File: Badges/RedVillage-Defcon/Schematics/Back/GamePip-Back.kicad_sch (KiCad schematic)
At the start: 21 parts

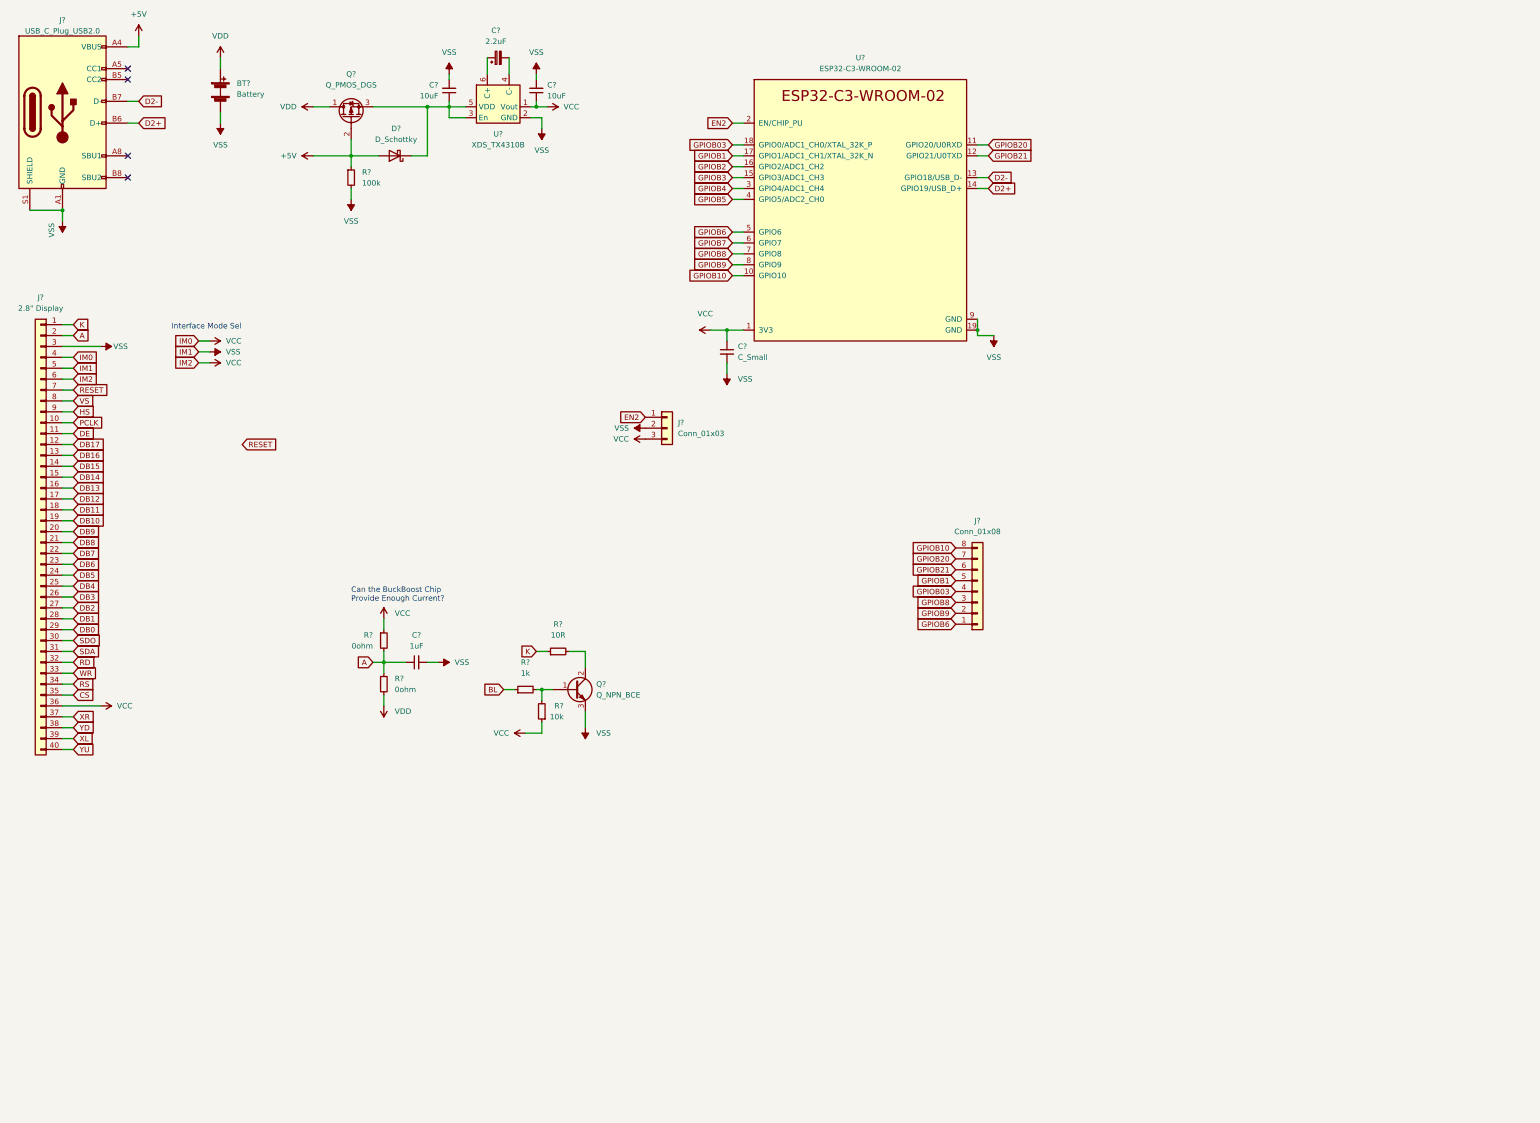
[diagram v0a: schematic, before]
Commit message: Changed RedVillage to ESP32-S2
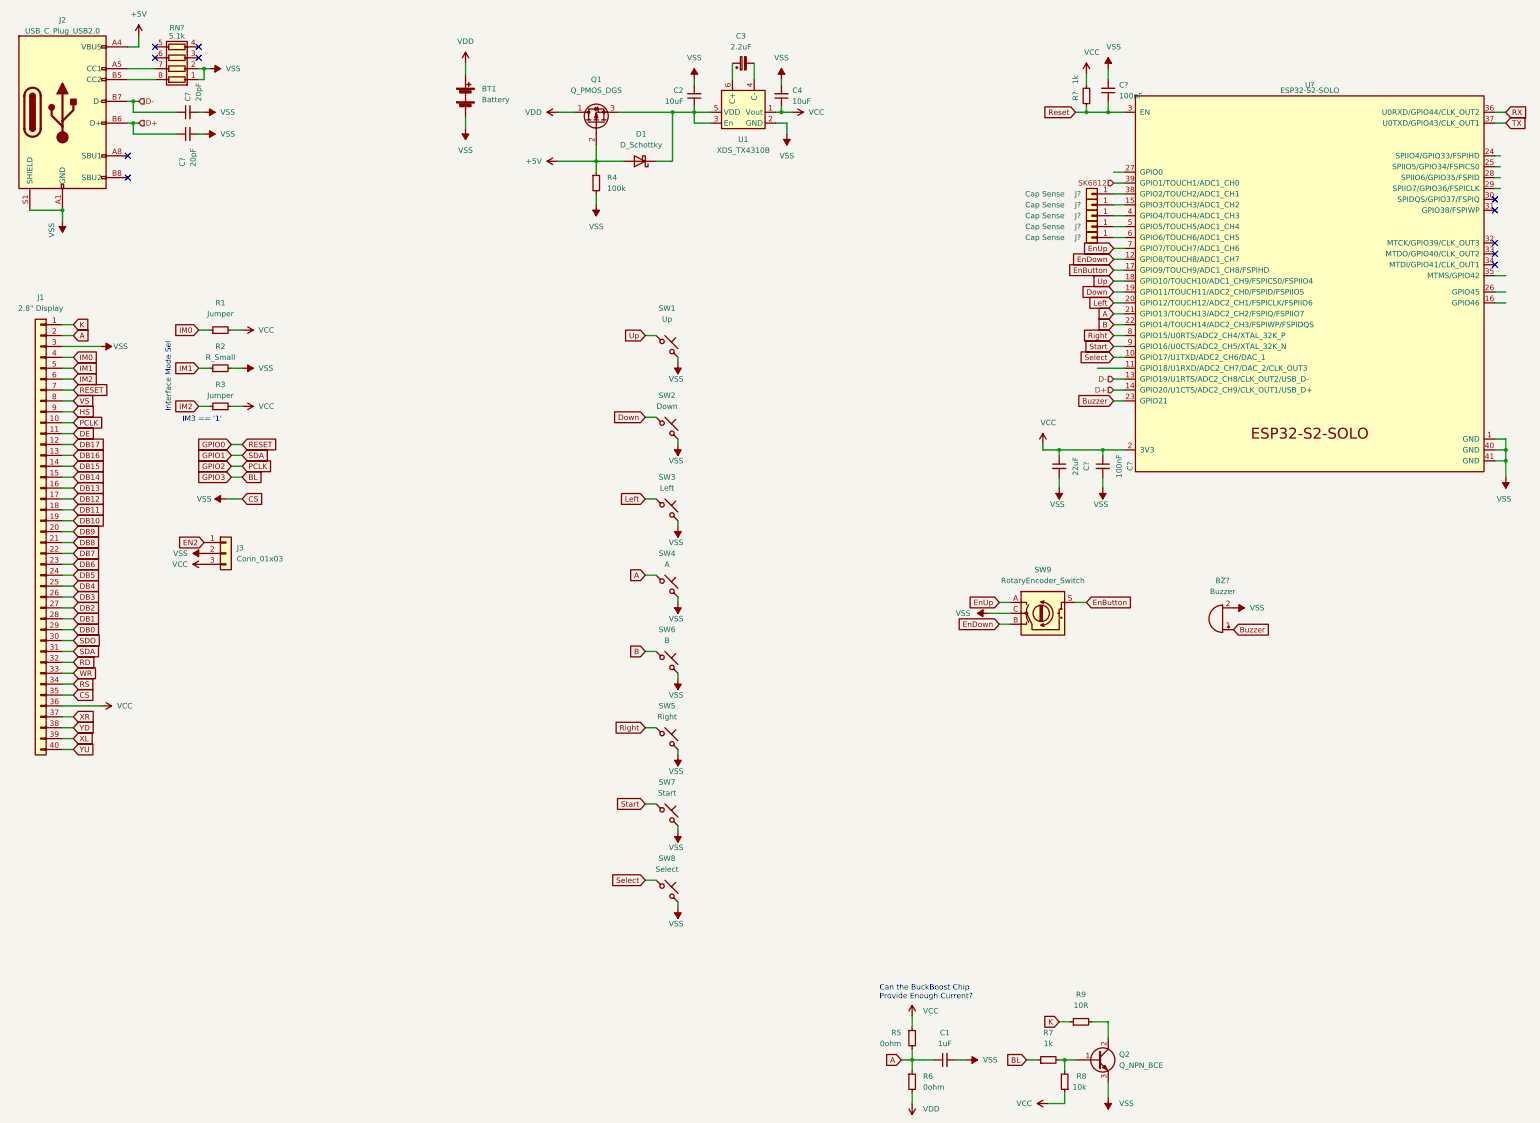
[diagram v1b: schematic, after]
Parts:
- removed C?: C_Small, Capacitor_SMD:C_0805_2012Metric, symbol Device:C_Small
- removed J?: Conn_01x08, Connector_PinHeader_2.54mm:PinHeader_1x08_P2.54mm_Vertical, symbol Connector_Generic:Conn_01x08
- removed U?: ESP32-C3-WROOM-02, Espressif:ESP32-C3-WROOM-02, symbol Espressif:ESP32-C3-WROOM-02
- added BZ?: Buzzer, Bsides22:FUET-9032-Buzzer, symbol Device:Buzzer
- added C? (x2): 100nF, Capacitor_SMD:C_0805_2012Metric, symbol Device:C_Small
- added C?: 22uF, Capacitor_SMD:C_0805_2012Metric, symbol Device:C_Small
- added C? (x2): 20pF, Capacitor_SMD:C_0805_2012Metric, symbol Device:C_Small
- added J? (x4): Cap Sense, Bsides22:CapSense, symbol Connector_Generic:Conn_01x01
- added J?: Cap Sense, CornConStranger:CapSence, symbol Connector_Generic:Conn_01x01
- added R1, R3: Jumper, symbol Device:R_Small
- added R2: R_Small, symbol Device:R_Small
- added R?: 1k, Resistor_SMD:R_0805_2012Metric, symbol Device:R_Small
- added RN?: 5.1k, Resistor_SMD:R_Array_Convex_4x0603, symbol Device:R_Pack04
- added SW1: Up, symbol Switch:SW_Push_45deg
- added SW2: Down, symbol Switch:SW_Push_45deg
- added SW3: Left, symbol Switch:SW_Push_45deg
- added SW4: A, symbol Switch:SW_Push_45deg
- added SW5: Right, symbol Switch:SW_Push_45deg
- added SW6: B, symbol Switch:SW_Push_45deg
- added SW7: Start, symbol Switch:SW_Push_45deg
- added SW8: Select, symbol Switch:SW_Push_45deg
- added SW9: RotaryEncoder_Switch, symbol RedVillage:RotaryEncoder_Switch
- added U?: ESP32-S2-SOLO, Espressif:ESP32-S2-SOLO, symbol Espressif:ESP32-S2-SOLO
- gave numbers to parts that had none: 18
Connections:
- net CS is gone; now on net VSS: J1.35 (Pin_35)
- net A: now also SW4.1, U?.21 (GPIO13/TOUCH13/ADC2_CH2/FSPIQ/FSPIIO7)
- net VCC: now also C?.1, C?.1, R1.2, R3.2, R?.2, U?.2 (3V3); no longer J1.4 (Pin_4), J1.6 (Pin_6)
- net VSS: now also BZ?.2 (+), C?.2, C?.2, C?.2, C?.2, C?.2, R2.2, RN?.1 (R1.1), RN?.2 (R2.1), SW1.2, SW2.2, SW3.2, SW4.2, SW5.2, SW6.2, SW7.2, SW8.2, SW9.C, U?.1 (GND), U?.40 (GND), U?.41 (GND); no longer J1.5 (Pin_5)
- net at J2.A5 (CC1): now also RN?.7 (R2.2)
- net at J2.B5 (CC2): now also RN?.8 (R1.2)
- net D2+ renamed D+
- net D+: now also C?.1, U?.14 (GPIO20/U1CTS/ADC2_CH9/CLK_OUT1/USB_D+)
- net D2- renamed D-
- net D-: now also C?.1, U?.13 (GPIO19/U1RTS/ADC2_CH8/CLK_OUT2/USB_D-)
- net PCLK renamed GPIO2
- net RESET renamed GPIO0
- net SDA renamed GPIO1
- new net: J?.1 (Pin_1), U?.6 (GPIO6/TOUCH6/ADC1_CH5)
- new net: J?.1 (Pin_1), U?.15 (GPIO3/TOUCH3/ADC1_CH2)
- new net: J?.1 (Pin_1), U?.38 (GPIO2/TOUCH2/ADC1_CH1)
- new net: J?.1 (Pin_1), U?.5 (GPIO5/TOUCH5/ADC1_CH4)
- new net: J?.1 (Pin_1), U?.4 (GPIO4/TOUCH4/ADC1_CH3)
- new net B: SW6.1, U?.22 (GPIO14/TOUCH14/ADC2_CH3/FSPIWP/FSPIDQS)
- new net Buzzer: BZ?.1 (-), U?.23 (GPIO21)
- new net Down: SW2.1, U?.19 (GPIO11/TOUCH11/ADC2_CH0/FSPID/FSPIIO5)
- new net EnButton: SW9.S, U?.17 (GPIO9/TOUCH9/ADC1_CH8/FSPIHD)
- new net EnDown: SW9.B, U?.12 (GPIO8/TOUCH8/ADC1_CH7)
- new net EnUp: SW9.A, U?.7 (GPIO7/TOUCH7/ADC1_CH6)
- new net IM0: J1.4 (Pin_4), R1.1
- new net IM1: J1.5 (Pin_5), R2.1
- new net IM2: J1.6 (Pin_6), R3.1
- new net Left: SW3.1, U?.20 (GPIO12/TOUCH12/ADC2_CH1/FSPICLK/FSPIIO6)
- new net RX: U?.36 (U0RXD/GPIO44/CLK_OUT2)
- new net Reset: C?.1, R?.1, U?.3 (EN)
- new net Right: SW5.1, U?.8 (GPIO15/U0RTS/ADC2_CH4/XTAL_32K_P)
- new net SK6812: U?.39 (GPIO1/TOUCH1/ADC1_CH0)
- new net Select: SW8.1, U?.10 (GPIO17/U1TXD/ADC2_CH6/DAC_1)
- new net Start: SW7.1, U?.9 (GPIO16/U0CTS/ADC2_CH5/XTAL_32K_N)
- new net TX: U?.37 (U0TXD/GPIO43/CLK_OUT1)
- new net Up: SW1.1, U?.18 (GPIO10/TOUCH10/ADC1_CH9/FSPICS0/FSPIIO4)
- no-connect marks 4 -> 11
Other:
- note added: "IM3 == '1'"
- moved on the sheet: BT1, C1, C2, C3, C4, D1, J3, Q1, Q2, R4, R5, R6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
